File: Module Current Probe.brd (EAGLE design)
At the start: 82.5 x 40.6 mm, 9 parts, among them J1 CON_HEADER_2X08-PTH-SHROUDED, J2 CON_HEADER_2X08-PTH-SHROUDED, J3 BANANA-JACK, J4 BANANA-JACK, J5 BANANA-JACK, J6 BANANA-JACK, J7 BANANA-JACK, J8 BANANA-JACK

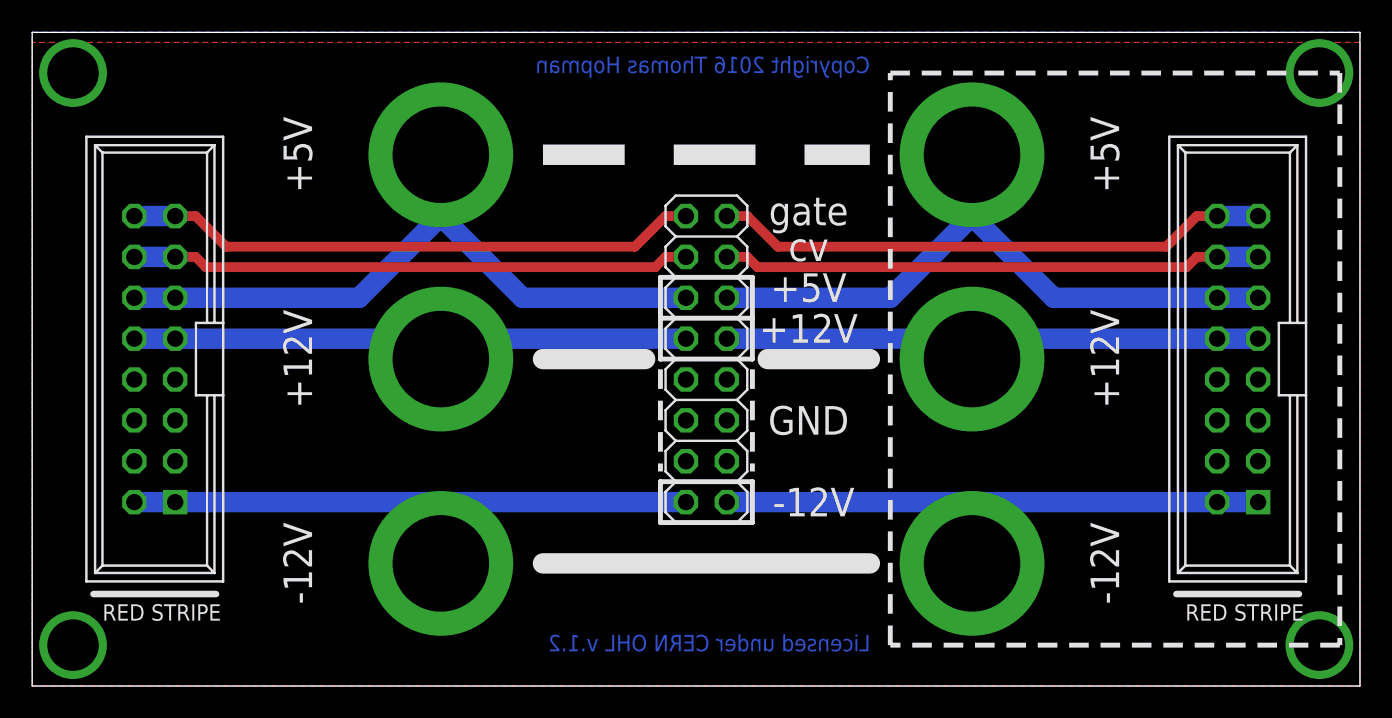
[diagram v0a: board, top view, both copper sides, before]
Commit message: Added ground connection for connecting a lab power supply.
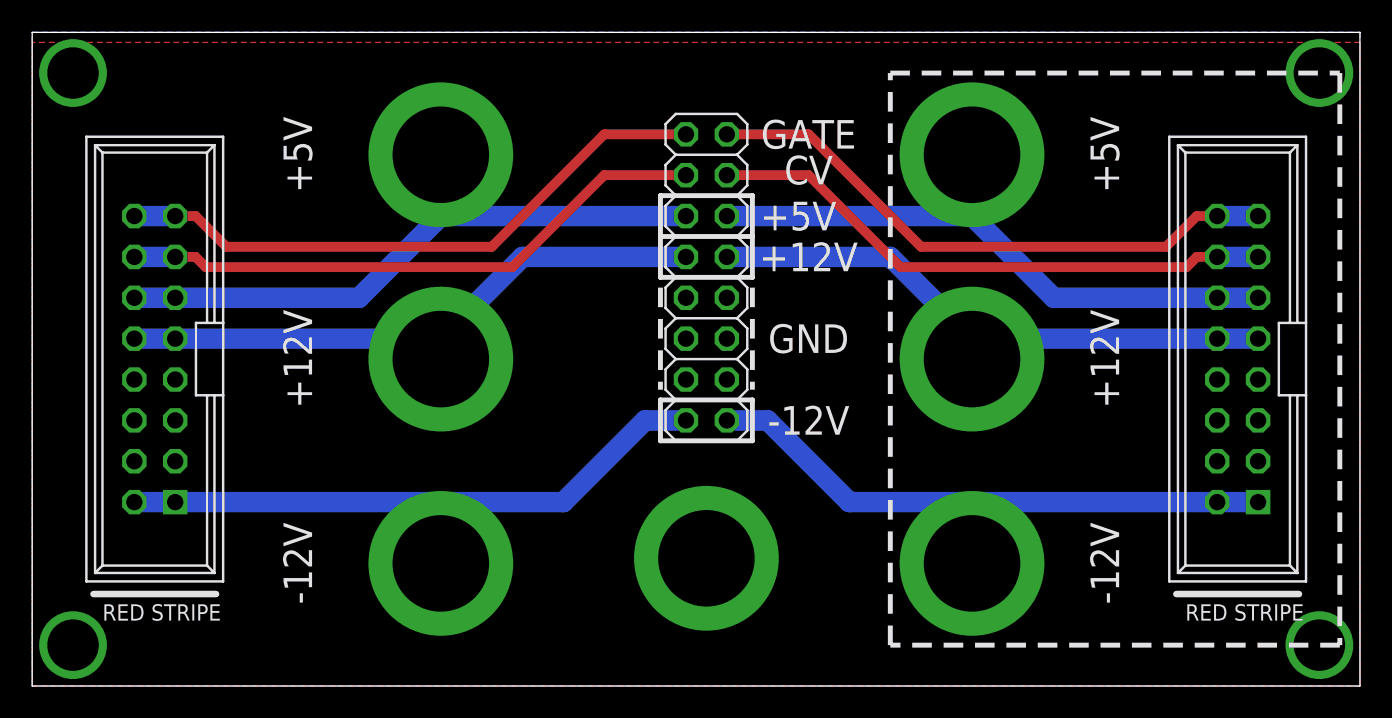
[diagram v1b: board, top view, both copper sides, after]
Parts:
- added J9: BANANA-JACK, con-banana:BANANA-PRINT
- moved JP1 5.08 mm to (41.9, 25.4)
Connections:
- net GND: now also J9.P$1
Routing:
- net -12VOUT: track 36.8 -> 38.9 mm
- net -12V: track 38.1 -> 40.2 mm
- net GATEOUT: track 34.6 -> 36.7 mm
- net CVOUT: track 33.5 -> 35.7 mm
- net CV: track 34.8 -> 36.9 mm
- net +5VOUT: track 41.0 -> 38.9 mm
- net +5V: track 42.3 -> 40.2 mm
- net +12VOUT: track 34.3 -> 36.4 mm
- net +12V: track 35.6 -> 37.7 mm
- net GATE: track 35.9 -> 38.0 mm
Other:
- board text added: "CV"
- board text added: "GATE"
- board text removed: "cv"
- board text removed: "gate"
